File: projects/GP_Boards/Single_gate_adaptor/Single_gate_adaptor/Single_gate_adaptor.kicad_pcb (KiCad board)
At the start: 2 copper layers, 38 parts, among them J1 Conn_01x15, J2 Conn_01x08, J3 Conn_01x15, J4 Conn_01x08, J5 Conn_01x08, J6 Conn_01x02, U1 74LVC1G97, U10 74LVC1G98, U11 74LVC1G04, U12 74LVC1G14, U13 74LVC1G17, U14 74LVC1G125, U15 74LVC1G86, U16 LMV321, U2 74LVC1G98, U3 74LVC1G04, U4 74LVC1G14, U5 74LVC1G17, U6 74LVC1G125, U7 74LVC1G86, U8 LMV321, U9 74LVC1G97

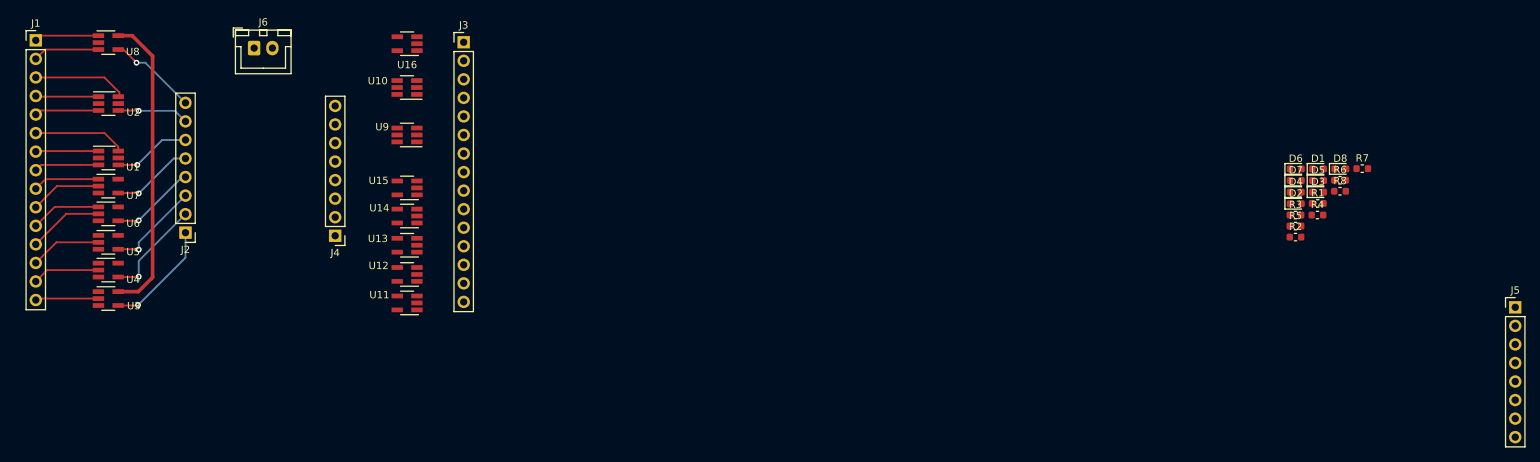
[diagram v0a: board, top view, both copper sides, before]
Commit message: added the GP boards
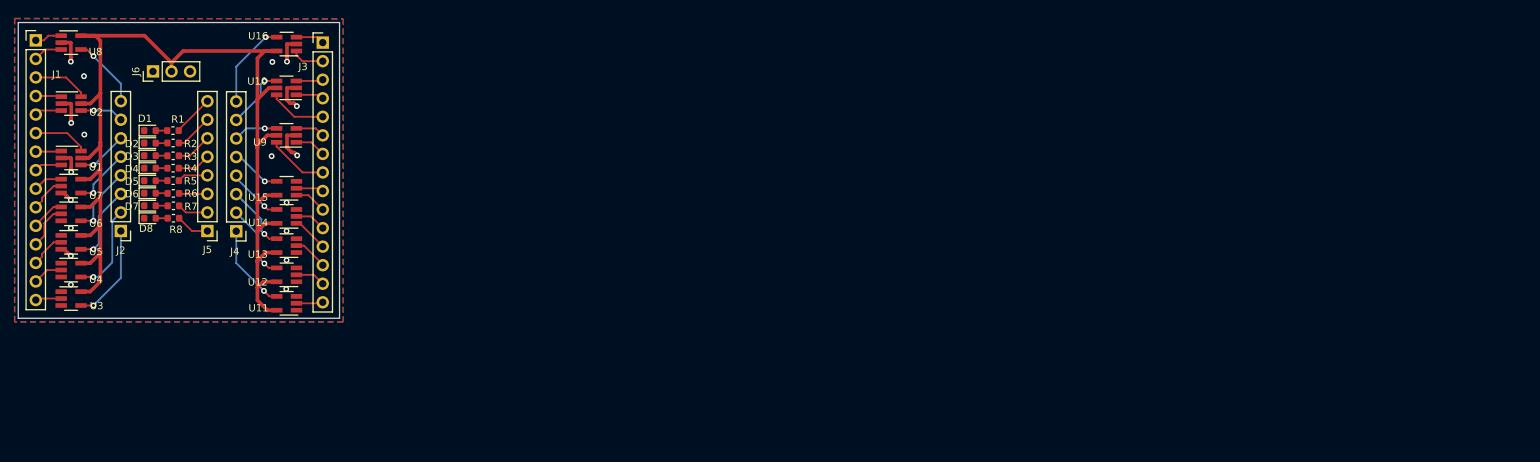
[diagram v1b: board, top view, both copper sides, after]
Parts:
- J6: value Conn_01x02 -> Conn_01x03; footprint Connector_JST:JST_XH_B02B-XH-A_1x02_P2.50mm_Vertical -> Connector_PinHeader_2.54mm:PinHeader_1x03_P2.54mm_Vertical
- moved J5 179.4 mm to (73.4, 78.0), turned to 180 degrees
- moved D8 163.1 mm to (65.5, 76.3)
- moved R7 162.9 mm to (68.8, 74.6)
- moved D1 160.0 mm to (65.5, 64.3)
- moved D3 160.0 mm to (65.5, 67.7)
- moved D5 160.0 mm to (65.5, 71.2)
- moved R8 159.8 mm to (68.8, 76.3)
- moved R6 159.8 mm to (68.7, 72.9)
- moved D2 157.1 mm to (65.5, 66.0)
- moved R1 157.1 mm to (68.7, 64.3)
- moved D7 156.9 mm to (65.5, 74.6)
- moved D6 156.9 mm to (65.5, 72.9)
- moved D4 156.9 mm to (65.5, 69.4)
- moved R4 156.8 mm to (68.7, 69.5)
- moved R2 154.2 mm to (68.7, 66.0)
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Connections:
- J6 pad 1: VCC -> (no net)
- J6 pad 2: GND -> VCC
- U10 pad 3: /C11 -> /C13
- U10 pad 6: /C13 -> /C11
- U9 pad 3: /C8 -> /C10
- U9 pad 6: /C10 -> /C8
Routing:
- net VCC: track 41.4 -> 148.4 mm
- net GND: track 0.00 -> 27.7 mm, vias 0 -> 18
- net /D8: track 0.00 -> 12.0 mm, vias 0 -> 1
- net /D1: track 0.00 -> 11.8 mm, vias 0 -> 1
- net /D2: track 0.00 -> 10.5 mm, vias 0 -> 1
- net /D3: track 0.00 -> 9.01 mm, vias 0 -> 1
- net /D7: track 0.00 -> 8.64 mm, vias 0 -> 1
- net /C8: track 0.00 -> 8.37 mm
- net /C11: track 0.00 -> 7.90 mm
- net /D4: track 0.00 -> 7.67 mm, vias 0 -> 1
- net /D5: track 0.00 -> 6.93 mm, vias 0 -> 1
- net /D6: track 0.00 -> 6.10 mm, vias 0 -> 1
- net Net-(J5-Pad8): track 0.00 -> 5.66 mm
- net /A14: track 9.33 -> 4.01 mm
- net /A13: track 12.9 -> 7.63 mm
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- added copper zone on B.Cu, net GND
- added copper zone on F.Cu, net GND
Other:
- board outline added: 44 x 40.5 mm
